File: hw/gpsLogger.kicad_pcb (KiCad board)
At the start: 2 copper layers, 41 x 72.8 mm, 163 parts, among them IC1 MSP430F55xx, P1 USB_OTG, P2 CONN_01X03, P3 CONN_01X03, Q1 Q_NMOS_AO8810, Q2 FG6943010R, SW1 SW_PUSH, SW2 SW_PUSH, U1 TPS27081A, U2 MCP73812, U3 uSD, U4 TPS27081A, U5 S8261, U6 TPS78230, X1 CRYSTAL_SMD

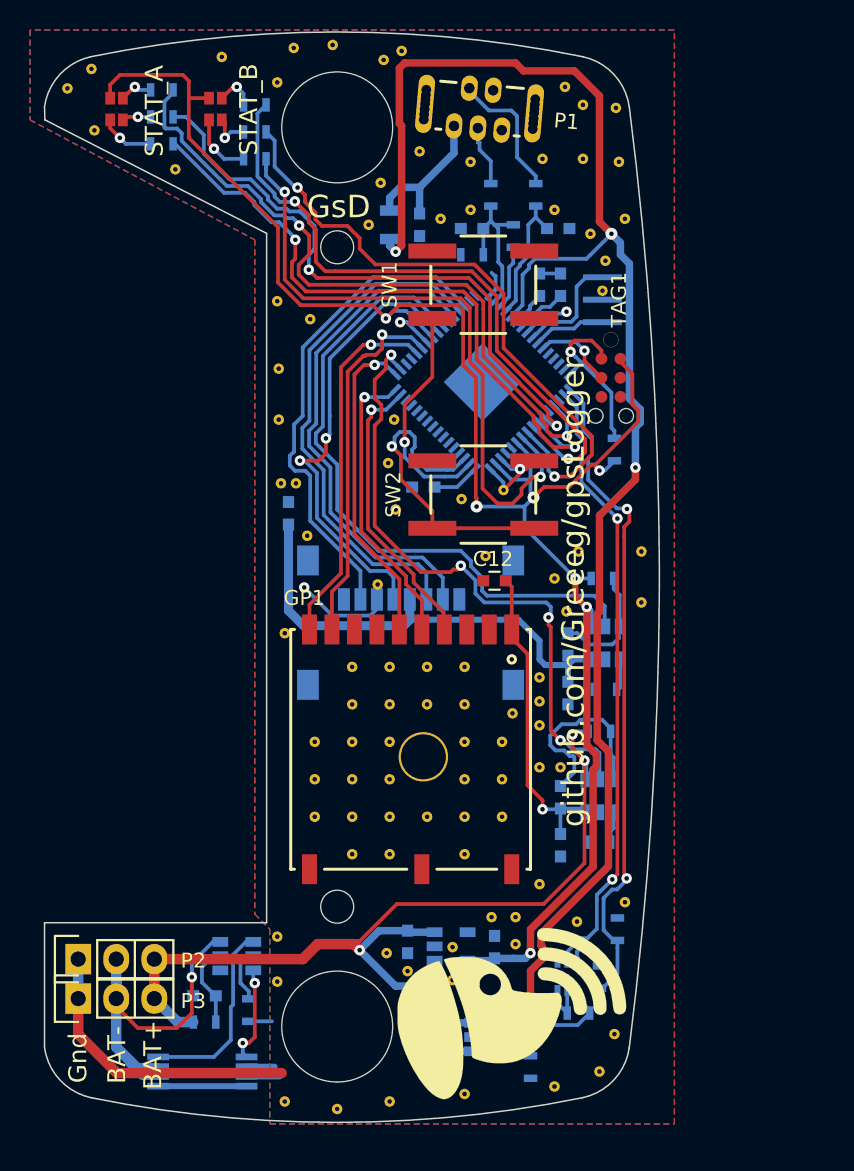
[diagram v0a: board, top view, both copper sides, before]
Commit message: 'Merge' Hardware changes mistakely made on Mark3 branch
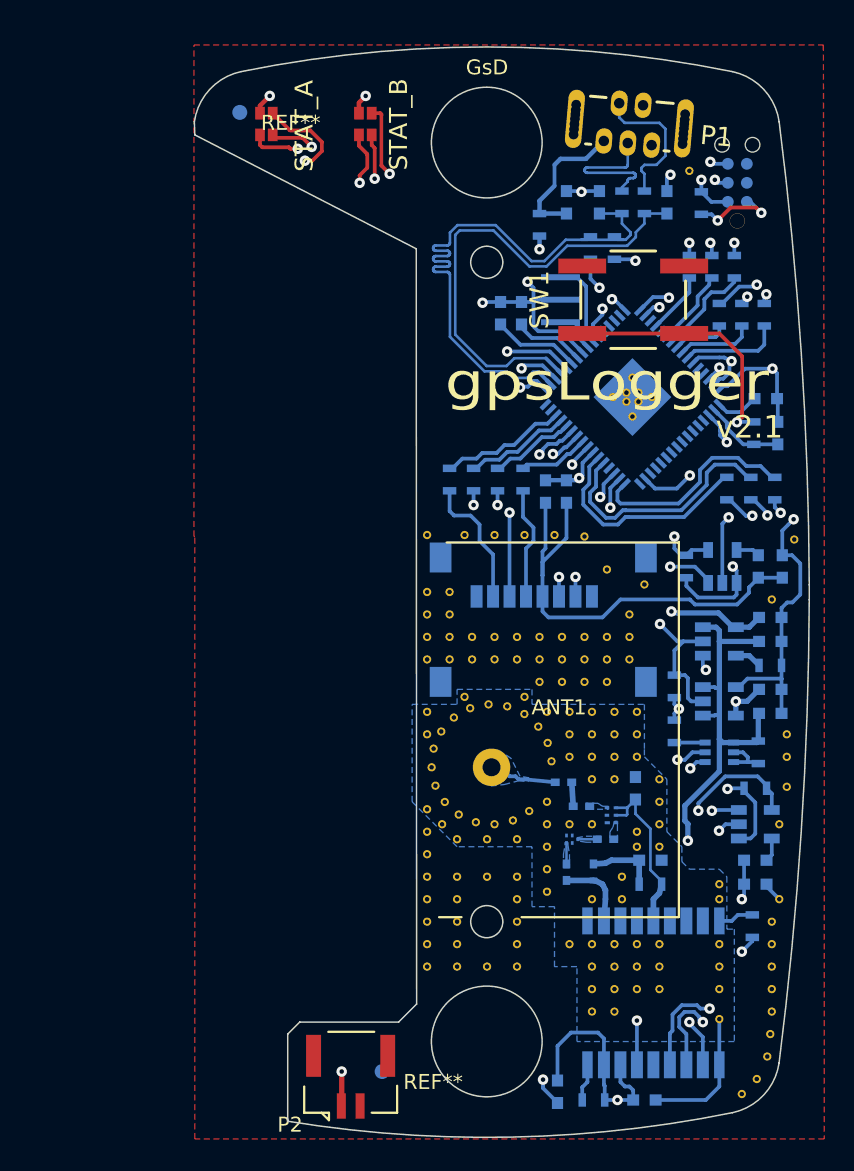
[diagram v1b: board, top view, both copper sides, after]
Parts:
- removed G*** (x2): LOGO, LOGO
- removed GP1: GPS, footprints:PA6C
- removed P3: CONN_01X03, Socket_Strips:Socket_Strip_Straight_1x03
- removed Q1: Q_NMOS_AO8810, Housings_SSOP:TSSOP-8_4.4x3mm_Pitch0.65mm
- removed the REF** at (160.7, 123.2)
- removed the REF** at (160.7, 77.6)
- removed the REF** at (141.5, 123.5)
- removed the REF** at (141.5, 79.5)
- removed the REF** at (141.5, 131.5)
- removed the REF** at (141.5, 71.5)
- removed the REF** at (160.1, 70.2)
- removed the REF** at (160.3, 73.8)
- removed the REF** at (157.9, 73.6)
- removed the REF** at (157.9, 70.0)
- removed the REF** at (156.7, 68.8)
- removed the REF** at (137.6, 87.6)
- removed the REF** at (137.6, 91.0)
- removed the REF** at (137.5, 83.1)
- removed the REF** at (139.7, 84.3)
- removed the REF** at (137.5, 68.5)
- removed the REF** at (145.3, 91.0)
- removed the REF** at (144.9, 93.9)
- removed the REF** at (145.4, 97.0)
- removed the REF** at (149.8, 96.3)
- removed the REF** at (152.6, 95.7)
- removed the REF** at (157.5, 124.5)
- removed the REF** at (155.0, 122.0)
- removed the REF** at (137.5, 125.5)
- removed the REF** at (137.5, 128.5)
- removed the REF** at (160.0, 132.0)
- removed the REF** at (130.7, 74.3)
- removed the REF** at (159.0, 134.5)
- removed the REF** at (156.0, 135.5)
- removed the REF** at (150.0, 136.0)
- removed the REF** at (145.0, 136.5)
- removed the REF** at (141.5, 137.0)
- removed the REF** at (138.0, 136.5)
- removed the REF** at (150.0, 107.5)
- removed the REF** at (152.5, 115.0)
- removed the REF** at (152.5, 112.5)
- removed the REF** at (145.0, 112.5)
- removed the REF** at (125.3, 71.7)
- removed the REF** at (142.5, 112.5)
- removed the REF** at (140.0, 112.5)
- removed the REF** at (142.5, 110.0)
- removed the REF** at (145.0, 110.0)
- removed the REF** at (147.5, 110.0)
- removed the REF** at (150.0, 110.0)
- removed the REF** at (150.0, 112.5)
- removed the REF** at (150.0, 115.0)
- removed the REF** at (145.0, 115.0)
- removed the REF** at (142.5, 115.0)
- removed the REF** at (123.5, 68.9)
- removed the REF** at (152.5, 117.5)
- removed the REF** at (150.0, 117.5)
- removed the REF** at (147.5, 117.5)
- removed the REF** at (145.0, 117.5)
- removed the REF** at (142.5, 117.5)
- removed the REF** at (145.0, 120.0)
- removed the REF** at (142.5, 120.0)
- removed the REF** at (138.6, 66.2)
- removed the REF** at (141.2, 66.0)
- removed the REF** at (145.8, 66.4)
- removed the REF** at (125.1, 67.6)
- removed the REF** at (144.6, 67.0)
- removed the REF** at (144.4, 75.2)
- removed the REF** at (143.6, 78.0)
- removed the REF** at (155.2, 73.6)
- removed the REF** at (150.4, 73.8)
- removed the REF** at (150.4, 77.0)
- removed the REF** at (156.0, 77.0)
- removed the REF** at (158.4, 78.6)
- removed the REF** at (159.2, 82.4)
- removed the REF** at (159.4, 80.4)
- removed the REF** at (133.8, 66.8)
- removed the REF** at (156.0, 101.6)
- removed the REF** at (157.6, 99.8)
- removed the REF** at (161.8, 103.2)
- removed the REF** at (161.8, 99.8)
- removed the REF** at (156.8, 103.8)
- removed the REF** at (150.0, 120.0)
- removed the REF** at (153.2, 110.6)
- removed the REF** at (155.0, 114.2)
- removed the REF** at (156.4, 114.2)
- removed the REF** at (155.0, 111.4)
- removed the REF** at (148.4, 77.6)
- removed the REF** at (155.0, 109.8)
- removed the REF** at (155.0, 108.2)
- removed the REF** at (153.4, 124.2)
- removed the REF** at (153.4, 126.0)
- removed the REF** at (151.8, 124.2)
- removed the REF** at (149.2, 128.4)
- removed the REF** at (149.2, 126.2)
- removed the REF** at (146.2, 127.8)
- removed the REF** at (144.8, 126.6)
- removed the REF** at (147.5, 107.5)
- removed the REF** at (147.0, 73.1)
- removed the REF** at (142.5, 107.5)
- removed the REF** at (145.0, 107.5)
- removed the REF** at (138.0, 105.2)
- removed the REF** at (137.8, 95.2)
- removed the REF** at (138.8, 95.2)
- removed the REF** at (139.5, 98.8)
- removed the REF** at (151.4, 100.1)
- removed the REF** at (144.2, 102.0)
- removed the REF** at (140.0, 115.0)
- removed the REF** at (140.0, 117.5)
- removed SW2: SW_PUSH, cameraTrigger_rev1_0:EVQ_switch
- added ANT1: ANT, footprints:GPS_ANT, F.Cu at (151.8, 114.2)
- added C18: 100n, Capacitors_SMD:C_0603, B.Cu at (155.4, 95.8)
- added C19: 47pF, Capacitors_SMD:C_0402, B.Cu at (156.6, 115.2)
- added C20: 1nF, Capacitors_SMD:C_0603, B.Cu at (161.4, 115.6)
- added C21: 47pF, Capacitors_SMD:C_0402, B.Cu at (159.4, 119.0)
- added C22: 47pF, Capacitors_SMD:C_0402, B.Cu at (156.8, 121.2)
- added FLT1: B8813, footprints:SAW-5, B.Cu at (157.2, 119.0)
- added L1: 27nH, Capacitors_SMD:C_0402, B.Cu at (158.6, 121.2)
- added L2: 100nH, Capacitors_SMD:C_0603, B.Cu at (169.4, 120.4)
- added L3: 100nH, Capacitors_SMD:C_0603, B.Cu at (169.6, 100.8)
- added L4: 5.6nH, Capacitors_SMD:C_0402, B.Cu at (157.8, 116.8)
- added R22: 2k2, Resistors_SMD:R_0603, B.Cu at (149.0, 95.0)
- added R23: 2k2, Resistors_SMD:R_0603, B.Cu at (150.6, 95.0)
- added R24: 2k2, Resistors_SMD:R_0603, B.Cu at (152.2, 95.0)
- added R25: 2k2, Resistors_SMD:R_0603, B.Cu at (153.9, 95.0)
- added R26: 2k2, Resistors_SMD:R_0603, B.Cu at (167.5, 95.6)
- added R27: 2k2, Resistors_SMD:R_0603, B.Cu at (169.1, 95.6)
- added R28: 2k2, Resistors_SMD:R_0603, B.Cu at (170.7, 95.6)
- added REF**: Fiducial_1mm_Dia_2.54mm_Outer_CopperBottom, Fiducials:Fiducial_1mm_Dia_2.54mm_Outer_CopperBottom, F.Cu at (144.5, 134.5)
- added REF**: SolderWirePad_single_0-8mmDrill, Wire_Pads:SolderWirePad_single_0-8mmDrill, F.Cu at (165.0, 74.4)
- added REF**: Fiducial_1mm_Dia_2.54mm_Outer_CopperBottom, Fiducials:Fiducial_1mm_Dia_2.54mm_Outer_CopperBottom, F.Cu at (135.0, 70.5)
- added REF**1: SolderWirePad_single_0-8mmDrill, Wire_Pads:SolderWirePad_single_0-8mmDrill, F.Cu at (160.8, 89.8)
- added REF**1: SolderWirePad_single_0-8mmDrill, Wire_Pads:SolderWirePad_single_0-8mmDrill, F.Cu at (155.0, 108.5)
- added REF**1: SolderWirePad_single_0-8mmDrill, Wire_Pads:SolderWirePad_single_0-8mmDrill, F.Cu at (147.5, 117.0)
- added REF**1: SolderWirePad_single_0-8mmDrill, Wire_Pads:SolderWirePad_single_0-8mmDrill, F.Cu at (148.5, 118.0)
- added REF**1: SolderWirePad_single_0-8mmDrill, Wire_Pads:SolderWirePad_single_0-8mmDrill, F.Cu at (149.5, 119.0)
- added REF**1: SolderWirePad_single_0-8mmDrill, Wire_Pads:SolderWirePad_single_0-8mmDrill, F.Cu at (151.5, 119.0)
- added REF**1: SolderWirePad_single_0-8mmDrill, Wire_Pads:SolderWirePad_single_0-8mmDrill, F.Cu at (153.5, 119.0)
- added REF**1: SolderWirePad_single_0-8mmDrill, Wire_Pads:SolderWirePad_single_0-8mmDrill, F.Cu at (155.5, 122.5)
- added REF**1: SolderWirePad_single_0-8mmDrill, Wire_Pads:SolderWirePad_single_0-8mmDrill, F.Cu at (155.5, 121.0)
- added REF**1: SolderWirePad_single_0-8mmDrill, Wire_Pads:SolderWirePad_single_0-8mmDrill, F.Cu at (155.5, 119.5)
- added REF**1: SolderWirePad_single_0-8mmDrill, Wire_Pads:SolderWirePad_single_0-8mmDrill, F.Cu at (158.5, 123.0)
- added REF**1: SolderWirePad_single_0-8mmDrill, Wire_Pads:SolderWirePad_single_0-8mmDrill, F.Cu at (160.5, 121.5)
- added REF**1: SolderWirePad_single_0-8mmDrill, Wire_Pads:SolderWirePad_single_0-8mmDrill, F.Cu at (159.5, 108.5)
- added REF**1: SolderWirePad_single_0-8mmDrill, Wire_Pads:SolderWirePad_single_0-8mmDrill, F.Cu at (160.5, 123.0)
- added REF**1: SolderWirePad_single_0-8mmDrill, Wire_Pads:SolderWirePad_single_0-8mmDrill, F.Cu at (155.5, 116.5)
- added REF**1: SolderWirePad_single_0-8mmDrill, Wire_Pads:SolderWirePad_single_0-8mmDrill, F.Cu at (155.5, 118.0)
- added REF**1: SolderWirePad_single_0-8mmDrill, Wire_Pads:SolderWirePad_single_0-8mmDrill, F.Cu at (157.0, 118.0)
- added REF**1: SolderWirePad_single_0-8mmDrill, Wire_Pads:SolderWirePad_single_0-8mmDrill, F.Cu at (158.5, 118.0)
- added REF**1: SolderWirePad_single_0-8mmDrill, Wire_Pads:SolderWirePad_single_0-8mmDrill, F.Cu at (161.5, 118.5)
- added REF**1: SolderWirePad_single_0-8mmDrill, Wire_Pads:SolderWirePad_single_0-8mmDrill, F.Cu at (161.5, 119.5)
- added REF**1: SolderWirePad_single_0-8mmDrill, Wire_Pads:SolderWirePad_single_0-8mmDrill, F.Cu at (163.0, 119.5)
- added REF**1: SolderWirePad_single_0-8mmDrill, Wire_Pads:SolderWirePad_single_0-8mmDrill, F.Cu at (163.0, 118.0)
- added REF**1: SolderWirePad_single_0-8mmDrill, Wire_Pads:SolderWirePad_single_0-8mmDrill, F.Cu at (163.0, 116.5)
- added REF**1: SolderWirePad_single_0-8mmDrill, Wire_Pads:SolderWirePad_single_0-8mmDrill, F.Cu at (158.0, 108.5)
- added REF**1: SolderWirePad_single_0-8mmDrill, Wire_Pads:SolderWirePad_single_0-8mmDrill, F.Cu at (163.0, 115.0)
- added REF**1: SolderWirePad_single_0-8mmDrill, Wire_Pads:SolderWirePad_single_0-8mmDrill, F.Cu at (160.0, 115.0)
- added REF**1: SolderWirePad_single_0-8mmDrill, Wire_Pads:SolderWirePad_single_0-8mmDrill, F.Cu at (158.5, 115.0)
- added REF**1: SolderWirePad_single_0-8mmDrill, Wire_Pads:SolderWirePad_single_0-8mmDrill, F.Cu at (157.0, 113.5)
- added REF**1: SolderWirePad_single_0-8mmDrill, Wire_Pads:SolderWirePad_single_0-8mmDrill, F.Cu at (158.5, 113.5)
- added REF**1: SolderWirePad_single_0-8mmDrill, Wire_Pads:SolderWirePad_single_0-8mmDrill, F.Cu at (160.0, 113.5)
- added REF**1: SolderWirePad_single_0-8mmDrill, Wire_Pads:SolderWirePad_single_0-8mmDrill, F.Cu at (161.5, 113.5)
- added REF**1: SolderWirePad_single_0-8mmDrill, Wire_Pads:SolderWirePad_single_0-8mmDrill, F.Cu at (161.5, 112.0)
- added REF**1: SolderWirePad_single_0-8mmDrill, Wire_Pads:SolderWirePad_single_0-8mmDrill, F.Cu at (160.0, 112.0)
- added REF**1: SolderWirePad_single_0-8mmDrill, Wire_Pads:SolderWirePad_single_0-8mmDrill, F.Cu at (158.5, 112.0)
- added REF**1: SolderWirePad_single_0-8mmDrill, Wire_Pads:SolderWirePad_single_0-8mmDrill, F.Cu at (149.0, 102.5)
- added REF**1: SolderWirePad_single_0-8mmDrill, Wire_Pads:SolderWirePad_single_0-8mmDrill, F.Cu at (157.0, 112.0)
- added REF**1: SolderWirePad_single_0-8mmDrill, Wire_Pads:SolderWirePad_single_0-8mmDrill, F.Cu at (155.5, 110.5)
- added REF**1: SolderWirePad_single_0-8mmDrill, Wire_Pads:SolderWirePad_single_0-8mmDrill, F.Cu at (157.0, 110.5)
- added REF**1: SolderWirePad_single_0-8mmDrill, Wire_Pads:SolderWirePad_single_0-8mmDrill, F.Cu at (158.5, 110.5)
- added REF**1: SolderWirePad_single_0-8mmDrill, Wire_Pads:SolderWirePad_single_0-8mmDrill, F.Cu at (160.0, 110.5)
- added REF**1: SolderWirePad_single_0-8mmDrill, Wire_Pads:SolderWirePad_single_0-8mmDrill, F.Cu at (161.5, 110.5)
- added REF**1: SolderWirePad_single_0-8mmDrill, Wire_Pads:SolderWirePad_single_0-8mmDrill, F.Cu at (158.0, 98.8)
- added REF**1: SolderWirePad_single_0-8mmDrill, Wire_Pads:SolderWirePad_single_0-8mmDrill, F.Cu at (156.0, 98.7)
- added REF**1: SolderWirePad_single_0-8mmDrill, Wire_Pads:SolderWirePad_single_0-8mmDrill, F.Cu at (154.0, 98.7)
- added REF**1: SolderWirePad_single_0-8mmDrill, Wire_Pads:SolderWirePad_single_0-8mmDrill, F.Cu at (152.0, 98.7)
- added REF**1: SolderWirePad_single_0-8mmDrill, Wire_Pads:SolderWirePad_single_0-8mmDrill, F.Cu at (147.5, 102.5)
- added REF**1: SolderWirePad_single_0-8mmDrill, Wire_Pads:SolderWirePad_single_0-8mmDrill, F.Cu at (150.0, 98.7)
- added REF**1: SolderWirePad_single_0-8mmDrill, Wire_Pads:SolderWirePad_single_0-8mmDrill, F.Cu at (147.5, 98.7)
- added REF**1: SolderWirePad_single_0-8mmDrill, Wire_Pads:SolderWirePad_single_0-8mmDrill, F.Cu at (147.8, 114.2)
- added REF**1: SolderWirePad_single_0-8mmDrill, Wire_Pads:SolderWirePad_single_0-8mmDrill, F.Cu at (147.5, 104.0)
- added REF**1: SolderWirePad_single_0-8mmDrill, Wire_Pads:SolderWirePad_single_0-8mmDrill, F.Cu at (149.0, 104.0)
- added REF**1: SolderWirePad_single_0-8mmDrill, Wire_Pads:SolderWirePad_single_0-8mmDrill, F.Cu at (161.0, 104.0)
- added REF**1: SolderWirePad_single_0-8mmDrill, Wire_Pads:SolderWirePad_single_0-8mmDrill, F.Cu at (147.5, 107.0)
- added REF**1: SolderWirePad_single_0-8mmDrill, Wire_Pads:SolderWirePad_single_0-8mmDrill, F.Cu at (159.5, 107.0)
- added REF**1: SolderWirePad_single_0-8mmDrill, Wire_Pads:SolderWirePad_single_0-8mmDrill, F.Cu at (161.6, 89.8)
- added REF**1: SolderWirePad_single_0-8mmDrill, Wire_Pads:SolderWirePad_single_0-8mmDrill, F.Cu at (158.0, 107.0)
- added REF**1: SolderWirePad_single_0-8mmDrill, Wire_Pads:SolderWirePad_single_0-8mmDrill, F.Cu at (156.5, 107.0)
- added REF**1: SolderWirePad_single_0-8mmDrill, Wire_Pads:SolderWirePad_single_0-8mmDrill, F.Cu at (155.0, 107.0)
- added REF**1: SolderWirePad_single_0-8mmDrill, Wire_Pads:SolderWirePad_single_0-8mmDrill, F.Cu at (153.5, 107.0)
- added REF**1: SolderWirePad_single_0-8mmDrill, Wire_Pads:SolderWirePad_single_0-8mmDrill, F.Cu at (152.0, 107.0)
- added REF**1: SolderWirePad_single_0-8mmDrill, Wire_Pads:SolderWirePad_single_0-8mmDrill, F.Cu at (150.5, 107.0)
- added REF**1: SolderWirePad_single_0-8mmDrill, Wire_Pads:SolderWirePad_single_0-8mmDrill, F.Cu at (149.0, 107.0)
- added REF**1: SolderWirePad_single_0-8mmDrill, Wire_Pads:SolderWirePad_single_0-8mmDrill, F.Cu at (161.0, 107.0)
- added REF**1: SolderWirePad_single_0-8mmDrill, Wire_Pads:SolderWirePad_single_0-8mmDrill, F.Cu at (161.0, 105.5)
- added REF**1: SolderWirePad_single_0-8mmDrill, Wire_Pads:SolderWirePad_single_0-8mmDrill, F.Cu at (159.5, 105.5)
- added REF**1: SolderWirePad_single_0-8mmDrill, Wire_Pads:SolderWirePad_single_0-8mmDrill, F.Cu at (161.6, 89.2)
- added REF**1: SolderWirePad_single_0-8mmDrill, Wire_Pads:SolderWirePad_single_0-8mmDrill, F.Cu at (158.0, 105.5)
- added REF**1: SolderWirePad_single_0-8mmDrill, Wire_Pads:SolderWirePad_single_0-8mmDrill, F.Cu at (156.5, 105.5)
- added REF**1: SolderWirePad_single_0-8mmDrill, Wire_Pads:SolderWirePad_single_0-8mmDrill, F.Cu at (155.0, 105.5)
- added REF**1: SolderWirePad_single_0-8mmDrill, Wire_Pads:SolderWirePad_single_0-8mmDrill, F.Cu at (153.5, 105.5)
- added REF**1: SolderWirePad_single_0-8mmDrill, Wire_Pads:SolderWirePad_single_0-8mmDrill, F.Cu at (152.0, 105.5)
- added REF**1: SolderWirePad_single_0-8mmDrill, Wire_Pads:SolderWirePad_single_0-8mmDrill, F.Cu at (150.5, 105.5)
- added REF**1: SolderWirePad_single_0-8mmDrill, Wire_Pads:SolderWirePad_single_0-8mmDrill, F.Cu at (149.0, 105.5)
- added REF**1: SolderWirePad_single_0-8mmDrill, Wire_Pads:SolderWirePad_single_0-8mmDrill, F.Cu at (147.5, 105.5)
- added REF**1: SolderWirePad_single_0-8mmDrill, Wire_Pads:SolderWirePad_single_0-8mmDrill, F.Cu at (149.5, 124.5)
- added REF**1: SolderWirePad_single_0-8mmDrill, Wire_Pads:SolderWirePad_single_0-8mmDrill, F.Cu at (149.5, 123.0)
- added REF**1: SolderWirePad_single_0-8mmDrill, Wire_Pads:SolderWirePad_single_0-8mmDrill, F.Cu at (160.8, 89.2)
- added REF**1: SolderWirePad_single_0-8mmDrill, Wire_Pads:SolderWirePad_single_0-8mmDrill, F.Cu at (149.5, 121.5)
- added REF**1: SolderWirePad_single_0-8mmDrill, Wire_Pads:SolderWirePad_single_0-8mmDrill, F.Cu at (151.5, 121.5)
- added REF**1: SolderWirePad_single_0-8mmDrill, Wire_Pads:SolderWirePad_single_0-8mmDrill, F.Cu at (153.5, 121.5)
- added REF**1: SolderWirePad_single_0-8mmDrill, Wire_Pads:SolderWirePad_single_0-8mmDrill, F.Cu at (153.5, 123.0)
- added REF**1: SolderWirePad_single_0-8mmDrill, Wire_Pads:SolderWirePad_single_0-8mmDrill, F.Cu at (153.5, 124.5)
- added REF**1: SolderWirePad_single_0-8mmDrill, Wire_Pads:SolderWirePad_single_0-8mmDrill, F.Cu at (153.5, 126.0)
- added REF**1: SolderWirePad_single_0-8mmDrill, Wire_Pads:SolderWirePad_single_0-8mmDrill, F.Cu at (149.5, 126.0)
- added REF**1: SolderWirePad_single_0-8mmDrill, Wire_Pads:SolderWirePad_single_0-8mmDrill, F.Cu at (147.5, 118.5)
- added REF**1: SolderWirePad_single_0-8mmDrill, Wire_Pads:SolderWirePad_single_0-8mmDrill, F.Cu at (147.5, 120.0)
- added REF**1: SolderWirePad_single_0-8mmDrill, Wire_Pads:SolderWirePad_single_0-8mmDrill, F.Cu at (147.5, 121.5)
- added REF**1: SolderWirePad_single_0-8mmDrill, Wire_Pads:SolderWirePad_single_0-8mmDrill, F.Cu at (161.2, 90.8)
- added REF**1: SolderWirePad_single_0-8mmDrill, Wire_Pads:SolderWirePad_single_0-8mmDrill, F.Cu at (147.5, 123.0)
- added REF**1: SolderWirePad_single_0-8mmDrill, Wire_Pads:SolderWirePad_single_0-8mmDrill, F.Cu at (147.5, 124.5)
- added REF**1: SolderWirePad_single_0-8mmDrill, Wire_Pads:SolderWirePad_single_0-8mmDrill, F.Cu at (147.5, 126.0)
- added REF**1: SolderWirePad_single_0-8mmDrill, Wire_Pads:SolderWirePad_single_0-8mmDrill, F.Cu at (147.5, 127.5)
- added REF**1: SolderWirePad_single_0-8mmDrill, Wire_Pads:SolderWirePad_single_0-8mmDrill, F.Cu at (149.5, 127.5)
- added REF**1: SolderWirePad_single_0-8mmDrill, Wire_Pads:SolderWirePad_single_0-8mmDrill, F.Cu at (151.5, 127.5)
- added REF**1: SolderWirePad_single_0-8mmDrill, Wire_Pads:SolderWirePad_single_0-8mmDrill, F.Cu at (153.5, 127.5)
- added REF**1: SolderWirePad_single_0-8mmDrill, Wire_Pads:SolderWirePad_single_0-8mmDrill, F.Cu at (168.5, 136.0)
- added REF**1: SolderWirePad_single_0-8mmDrill, Wire_Pads:SolderWirePad_single_0-8mmDrill, F.Cu at (169.5, 135.0)
- added REF**1: SolderWirePad_single_0-8mmDrill, Wire_Pads:SolderWirePad_single_0-8mmDrill, F.Cu at (170.2, 133.5)
- added REF**1: SolderWirePad_single_0-8mmDrill, Wire_Pads:SolderWirePad_single_0-8mmDrill, F.Cu at (161.2, 88.2)
- added REF**1: SolderWirePad_single_0-8mmDrill, Wire_Pads:SolderWirePad_single_0-8mmDrill, F.Cu at (170.4, 132.0)
- added REF**1: SolderWirePad_single_0-8mmDrill, Wire_Pads:SolderWirePad_single_0-8mmDrill, F.Cu at (170.5, 130.5)
- added REF**1: SolderWirePad_single_0-8mmDrill, Wire_Pads:SolderWirePad_single_0-8mmDrill, F.Cu at (170.5, 129.0)
- added REF**1: SolderWirePad_single_0-8mmDrill, Wire_Pads:SolderWirePad_single_0-8mmDrill, F.Cu at (170.5, 127.5)
- added REF**1: SolderWirePad_single_0-8mmDrill, Wire_Pads:SolderWirePad_single_0-8mmDrill, F.Cu at (170.5, 126.0)
- added REF**1: SolderWirePad_single_0-8mmDrill, Wire_Pads:SolderWirePad_single_0-8mmDrill, F.Cu at (170.5, 124.5)
- added REF**1: SolderWirePad_single_0-8mmDrill, Wire_Pads:SolderWirePad_single_0-8mmDrill, F.Cu at (171.0, 123.0)
- added REF**1: SolderWirePad_single_0-8mmDrill, Wire_Pads:SolderWirePad_single_0-8mmDrill, F.Cu at (171.0, 118.0)
- added REF**1: SolderWirePad_single_0-8mmDrill, Wire_Pads:SolderWirePad_single_0-8mmDrill, F.Cu at (171.5, 115.5)
- added REF**1: SolderWirePad_single_0-8mmDrill, Wire_Pads:SolderWirePad_single_0-8mmDrill, F.Cu at (171.5, 113.5)
- added REF**1: SolderWirePad_single_0-8mmDrill, Wire_Pads:SolderWirePad_single_0-8mmDrill, F.Cu at (162.5, 89.5)
- added REF**1: SolderWirePad_single_0-8mmDrill, Wire_Pads:SolderWirePad_single_0-8mmDrill, F.Cu at (171.5, 112.0)
- added REF**1: SolderWirePad_single_0-8mmDrill, Wire_Pads:SolderWirePad_single_0-8mmDrill, F.Cu at (172.0, 99.0)
- added REF**1: SolderWirePad_single_0-8mmDrill, Wire_Pads:SolderWirePad_single_0-8mmDrill, F.Cu at (170.5, 103.0)
- added REF**1: SolderWirePad_single_0-8mmDrill, Wire_Pads:SolderWirePad_single_0-8mmDrill, F.Cu at (159.5, 101.0)
- added REF**1: SolderWirePad_single_0-8mmDrill, Wire_Pads:SolderWirePad_single_0-8mmDrill, F.Cu at (162.0, 102.0)
- added REF**1: SolderWirePad_single_0-8mmDrill, Wire_Pads:SolderWirePad_single_0-8mmDrill, F.Cu at (158.5, 130.5)
- added REF**1: SolderWirePad_single_0-8mmDrill, Wire_Pads:SolderWirePad_single_0-8mmDrill, F.Cu at (160.0, 130.5)
- added REF**1: SolderWirePad_single_0-8mmDrill, Wire_Pads:SolderWirePad_single_0-8mmDrill, F.Cu at (158.5, 129.0)
- added REF**1: SolderWirePad_single_0-8mmDrill, Wire_Pads:SolderWirePad_single_0-8mmDrill, F.Cu at (167.0, 129.0)
- added REF**1: SolderWirePad_single_0-8mmDrill, Wire_Pads:SolderWirePad_single_0-8mmDrill, F.Cu at (160.0, 129.0)
- added REF**1: SolderWirePad_single_0-8mmDrill, Wire_Pads:SolderWirePad_single_0-8mmDrill, F.Cu at (159.9, 89.5)
- added REF**1: SolderWirePad_single_0-8mmDrill, Wire_Pads:SolderWirePad_single_0-8mmDrill, F.Cu at (163.0, 129.0)
- added REF**1: SolderWirePad_single_0-8mmDrill, Wire_Pads:SolderWirePad_single_0-8mmDrill, F.Cu at (161.5, 129.0)
- added REF**1: SolderWirePad_single_0-8mmDrill, Wire_Pads:SolderWirePad_single_0-8mmDrill, F.Cu at (157.0, 126.0)
- added REF**1: SolderWirePad_single_0-8mmDrill, Wire_Pads:SolderWirePad_single_0-8mmDrill, F.Cu at (158.5, 127.5)
- added REF**1: SolderWirePad_single_0-8mmDrill, Wire_Pads:SolderWirePad_single_0-8mmDrill, F.Cu at (158.5, 126.0)
- added REF**1: SolderWirePad_single_0-8mmDrill, Wire_Pads:SolderWirePad_single_0-8mmDrill, F.Cu at (160.0, 127.5)
- added REF**1: SolderWirePad_single_0-8mmDrill, Wire_Pads:SolderWirePad_single_0-8mmDrill, F.Cu at (160.0, 126.0)
- added REF**1: SolderWirePad_single_0-8mmDrill, Wire_Pads:SolderWirePad_single_0-8mmDrill, F.Cu at (161.5, 127.5)
- added REF**1: SolderWirePad_single_0-8mmDrill, Wire_Pads:SolderWirePad_single_0-8mmDrill, F.Cu at (161.5, 126.0)
- added REF**1: SolderWirePad_single_0-8mmDrill, Wire_Pads:SolderWirePad_single_0-8mmDrill, F.Cu at (163.0, 127.5)
- added REF**1: SolderWirePad_single_0-8mmDrill, Wire_Pads:SolderWirePad_single_0-8mmDrill, F.Cu at (156.5, 108.5)
- added REF**1: SolderWirePad_single_0-8mmDrill, Wire_Pads:SolderWirePad_single_0-8mmDrill, F.Cu at (163.0, 126.0)
- added REF**1: SolderWirePad_single_0-8mmDrill, Wire_Pads:SolderWirePad_single_0-8mmDrill, F.Cu at (167.0, 131.0)
- added REF**1: SolderWirePad_single_0-8mmDrill, Wire_Pads:SolderWirePad_single_0-8mmDrill, F.Cu at (167.0, 127.5)
- added REF**1: SolderWirePad_single_0-8mmDrill, Wire_Pads:SolderWirePad_single_0-8mmDrill, F.Cu at (167.0, 126.0)
- added REF**1: SolderWirePad_single_0-8mmDrill, Wire_Pads:SolderWirePad_single_0-8mmDrill, F.Cu at (167.0, 123.0)
- added REF**1: SolderWirePad_single_0-8mmDrill, Wire_Pads:SolderWirePad_single_0-8mmDrill, F.Cu at (167.0, 122.0)
- added REF**1: SolderWirePad_single_0-8mmDrill, Wire_Pads:SolderWirePad_single_0-8mmDrill, F.Cu at (154.0, 109.5)
- added REF**1: SolderWirePad_single_0-8mmDrill, Wire_Pads:SolderWirePad_single_0-8mmDrill, F.Cu at (150.0, 109.5)
- added REF**1: SolderWirePad_single_0-8mmDrill, Wire_Pads:SolderWirePad_single_0-8mmDrill, F.Cu at (147.5, 112.0)
- added REF**1: SolderWirePad_single_0-8mmDrill, Wire_Pads:SolderWirePad_single_0-8mmDrill, F.Cu at (147.5, 110.5)
- added REF**11: SolderWirePad_single_0-8mmDrill, Wire_Pads:SolderWirePad_single_0-8mmDrill, F.Cu at (155.8, 113.8)
- added REF**12: SolderWirePad_single_0-8mmDrill, Wire_Pads:SolderWirePad_single_0-8mmDrill, F.Cu at (155.5, 112.6)
- added REF**13: SolderWirePad_single_0-8mmDrill, Wire_Pads:SolderWirePad_single_0-8mmDrill, F.Cu at (154.9, 111.5)
- added REF**14: SolderWirePad_single_0-8mmDrill, Wire_Pads:SolderWirePad_single_0-8mmDrill, F.Cu at (154.0, 110.6)
- added REF**15: SolderWirePad_single_0-8mmDrill, Wire_Pads:SolderWirePad_single_0-8mmDrill, F.Cu at (152.8, 110.1)
- added REF**16: SolderWirePad_single_0-8mmDrill, Wire_Pads:SolderWirePad_single_0-8mmDrill, F.Cu at (151.6, 110.0)
- added REF**17: SolderWirePad_single_0-8mmDrill, Wire_Pads:SolderWirePad_single_0-8mmDrill, F.Cu at (150.4, 110.3)
- added REF**18: SolderWirePad_single_0-8mmDrill, Wire_Pads:SolderWirePad_single_0-8mmDrill, F.Cu at (149.3, 110.9)
- added REF**19: SolderWirePad_single_0-8mmDrill, Wire_Pads:SolderWirePad_single_0-8mmDrill, F.Cu at (148.4, 111.8)
- added REF**2: SolderWirePad_single_0-8mmDrill, Wire_Pads:SolderWirePad_single_0-8mmDrill, F.Cu at (148.1, 115.4)
- added REF**20: SolderWirePad_single_0-8mmDrill, Wire_Pads:SolderWirePad_single_0-8mmDrill, F.Cu at (147.9, 113.0)
- added REF**3: SolderWirePad_single_0-8mmDrill, Wire_Pads:SolderWirePad_single_0-8mmDrill, F.Cu at (148.7, 116.5)
- added REF**4: SolderWirePad_single_0-8mmDrill, Wire_Pads:SolderWirePad_single_0-8mmDrill, F.Cu at (149.6, 117.4)
- added REF**5: SolderWirePad_single_0-8mmDrill, Wire_Pads:SolderWirePad_single_0-8mmDrill, F.Cu at (150.8, 117.9)
- added REF**6: SolderWirePad_single_0-8mmDrill, Wire_Pads:SolderWirePad_single_0-8mmDrill, F.Cu at (152.0, 118.0)
- added REF**7: SolderWirePad_single_0-8mmDrill, Wire_Pads:SolderWirePad_single_0-8mmDrill, F.Cu at (153.2, 117.7)
- added REF**8: SolderWirePad_single_0-8mmDrill, Wire_Pads:SolderWirePad_single_0-8mmDrill, F.Cu at (154.3, 117.1)
- added U7: BGU7007, footprints:XSON6, B.Cu at (159.8, 117.4)
- C1, C5, C7: value C -> 10n
- C10, C11: value C -> 100n
- C12: value C -> 10n; moved to B.Cu
- C13, C16, C17, C4, C8: value C -> 1uF
- C2, C3: value C -> 22p
- FB1: value FILTER -> 1k FB; footprint Resistors_SMD:R_0805 -> Resistors_SMD:R_0603
- P2: value CONN_01X03 -> CONN_01X02; footprint Socket_Strips:Socket_Strip_Straight_1x03 -> footprints:BM02B-GHS-TBT
- R1, R2: value R -> 27R
- R10: value R -> 1k
- R11: value 1K -> 10k
- R3: value R -> 470k
- R4: value R -> 1k4
- R5, R8: value R -> 10k
- R6: value R -> 10R
- R9: value 330R -> 10k
- TAG1: moved to B.Cu
- U1: value TPS27081A -> MAX_M8Q; footprint TO_SOT_Packages_SMD:SOT-23-6 -> footprints:MAX_M8
- U4: value TPS27081A -> MIC2091; footprint TO_SOT_Packages_SMD:SOT-23-6 -> TO_SOT_Packages_SMD:SOT-23-5
- U5: value S8261 -> MIC2091; footprint TO_SOT_Packages_SMD:SOT-23-6 -> TO_SOT_Packages_SMD:SOT-23-5
- moved C11 53.6 mm to (170.9, 91.9), turned to 90 degrees
- moved R11 41.6 mm to (164.8, 100.8)
- moved U5 41.5 mm to (167.2, 100.8), turned to 90 degrees
- moved R9 39.9 mm to (169.4, 115.6)
- moved R18 39.1 mm to (168.0, 80.8), turned to 270 degrees
- moved R17 38.0 mm to (166.5, 80.8), turned to 270 degrees
- moved C6 37.1 mm to (170.4, 104.2), turned to 0 degrees
- moved R16 37.1 mm to (165.0, 80.8), turned to 270 degrees
- moved C12 36.1 mm to (162.0, 136.4), turned to 0 degrees
- moved R21 35.6 mm to (170.0, 84.0), turned to 270 degrees
- moved R20 34.7 mm to (168.5, 84.0), turned to 270 degrees
- moved R19 34.0 mm to (167.0, 84.0), turned to 270 degrees
- moved C9 33.8 mm to (170.4, 105.8), turned to 0 degrees
- moved R7 31.2 mm to (170.4, 107.4), turned to 180 degrees
- moved U2 30.6 mm to (167.0, 105.8)
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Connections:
- net /D+ renamed /USB_IN_P
- net /D- renamed /USB_IN_N
- net /DM renamed /USB_DATA_N
- net /DP renamed /USB_DATA_P
- C10 pad 1: /GPS_VCC -> GPS_VCC
- C10 pad 2: Net-(C10-Pad2) -> GND
- C11 pad 1: Net-(C11-Pad1) -> PWR_BUT
- C11 pad 2: /BAT- -> GND
- C12 pad 1: /GPS_VCC -> GPS_VCC
- C13 pad 1: /GPS_VCC -> GPS_VCC
- C5 pad 1: /SD_VCC -> Net-(C5-Pad1)
- C5 pad 2: Net-(C5-Pad2) -> GND
- C7 pad 1: /SD_VCC -> MMC_VCC
- C8 pad 1: /SD_VCC -> MMC_VCC
- IC1 pad 18: /PWR_BUT -> PWR_BUT
- IC1 pad 19: /NEW_BUT -> ~CHG
- IC1 pad 31: /GPS_BACKUP -> GPS_BACKUP
- IC1 pad 32: /GPS_FIX -> Net-(IC1-Pad32)
- IC1 pad 33: /GPS_PPS -> Net-(IC1-Pad33)
- IC1 pad 34: /GPS_PWR -> GPS_PWR
- IC1 pad 35: Net-(IC1-Pad35) -> GPS_PWR_FAULT
- IC1 pad 37: /GPS_MOSI -> Net-(IC1-Pad37)
- IC1 pad 38: /GPS_MISO -> Net-(IC1-Pad38)
- IC1 pad 41: /SD_CLK -> Net-(IC1-Pad41)
- IC1 pad 42: /SD_PWR -> MMC_PWR
- IC1 pad 43: Net-(IC1-Pad43) -> MMC_PWR_FAULT
- IC1 pad 44: /SD_CS -> Net-(IC1-Pad44)
- IC1 pad 45: /SD_MOSI -> Net-(IC1-Pad45)
- IC1 pad 46: /SD_MISO -> Net-(IC1-Pad46)
- IC1 pad 65: (no net) -> GND
- P2 pad 1: GND -> +BATT
- P2 pad 2: /BAT- -> GND
- R10 pad 1: Net-(R10-Pad1) -> PWR_BUT
- R10 pad 2: GND -> Net-(R10-Pad2)
- R11 pad 1: Net-(R11-Pad1) -> MMC_PWR_FAULT
- R11 pad 2: GND -> +3V3
- R5 pad 1: Net-(C5-Pad2) -> Net-(R5-Pad1)
- R5 pad 2: +3V3 -> GPS_VCC
- R6 pad 1: Net-(R6-Pad1) -> GPS_VCC_RF
- R6 pad 2: GND -> Net-(C5-Pad1)
- R8 pad 1: Net-(C10-Pad2) -> GPS_VCC
- R8 pad 2: +BATT -> Net-(R8-Pad2)
- R9 pad 1: Net-(C11-Pad1) -> GPS_PWR_FAULT
- R9 pad 2: +BATT -> +3V3
- SW1 pad 1: /PWR_BUT -> Net-(R10-Pad2)
- U1 pad 1: Net-(R6-Pad1) -> GND
- U1 pad 2: /SD_VCC -> GPS_MISO
- U1 pad 3: /SD_VCC -> GPS_MOSI
- U1 pad 4: +3V3 -> GPS_PPS
- U1 pad 5: /SD_PWR -> Net-(U1-Pad5)
- U1 pad 6: Net-(C5-Pad2) -> GPS_BACKUP
- U2 pad 1: VBUS -> ~CHG
- U3 pad 2: /SD_CS -> MMC_CS
- U3 pad 3: /SD_MOSI -> MMC_MOSI
- U3 pad 4: /SD_VCC -> MMC_VCC
- U3 pad 5: /SD_CLK -> MMC_CLK
- U3 pad 7: /SD_MISO -> MMC_MISO
- U4 pad 1: Net-(R10-Pad1) -> +3V3
- U4 pad 2: /GPS_VCC -> GND
- U4 pad 3: /GPS_VCC -> GPS_PWR
- U4 pad 4: +BATT -> GPS_PWR_FAULT
- U4 pad 5: /GPS_PWR -> Net-(L2-Pad1)
- U5 pad 1: Net-(Q1-Pad4) -> +3V3
- U5 pad 2: Net-(R11-Pad1) -> GND
- U5 pad 3: Net-(Q1-Pad5) -> MMC_PWR
- U5 pad 4: Net-(U5-Pad4) -> MMC_PWR_FAULT
- U5 pad 5: Net-(C11-Pad1) -> Net-(L3-Pad1)
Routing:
- net VBUS: track 111.8 -> 44.1 mm, vias 4 -> 3
- net GPS_BACKUP: track 0.00 -> 49.1 mm, vias 0 -> 2
- net /SD_PWR: track 44.1 -> 0.00 mm
- net GPS_MOSI: track 0.00 -> 42.9 mm, vias 0 -> 2
- net GPS_PPS: track 0.00 -> 42.5 mm, vias 0 -> 2
- net /GPS_PWR: track 42.4 -> 0.00 mm, vias 4 -> 0
- net /LED_A_R: track 46.1 -> 4.14 mm, vias 2 -> 0
- net GPS_MISO: track 0.00 -> 41.6 mm, vias 0 -> 2
- net GND: track 48.0 -> 89.6 mm, vias 4 -> 17
- net /LED_B_R: track 43.4 -> 3.71 mm, vias 2 -> 0
- net GPS_VCC: track 0.00 -> 38.1 mm, vias 0 -> 3
- net GPS_PWR_FAULT: track 0.00 -> 37.9 mm, vias 0 -> 2
- net /LED_B_G: track 42.3 -> 5.15 mm, vias 2 -> 0
- net /LED_A_B: track 42.9 -> 6.50 mm, vias 2 -> 0
- net /LED_B_B: track 43.1 -> 6.74 mm, vias 2 -> 0
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- added copper zone on B.Cu, net /ANT_RF
- added copper zone on In2.Cu, net GND
- added copper zone on B.Cu, net Net-(C21-Pad1)
- added copper zone on B.Cu, net Net-(C21-Pad2)
- added copper zone on B.Cu, net Net-(C22-Pad2)
- added copper zone on B.Cu, net Net-(L4-Pad2)
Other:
- outline, holes or cut-outs redrawn
- copper layers 2 -> 4
- net class Power: clearance 0.2 -> 0.22
- net class USB added: clearance 0.177, trace_width 0.177, via_dia 0.7, via_drill 0.3
- rule trace_min: 0.18 -> 0.15
- board text added: "gpsLogger"
- board text added: "v2.1"
- board text removed: "BAT+"
- board text removed: "BAT-"
- board text removed: "Gnd"
- board text removed: "github.com/Greeeg/gpsLogger"

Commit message: Merge PCB changes from Mark3 branch.
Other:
- rule pad_to_mask_clearance: 0.2 -> 0.05
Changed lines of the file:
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@@
-(kicad_pcb (version 4) (host pcbnew 4.0.2-stable)
+(kicad_pcb (version 20171130) (host pcbnew "(5.0.0-rc2-dev-321-g78161b592)")
   (general
-    (links 342)
-    (no_connects 0)
-    (area -81.418183 56.392421 174.000001 148.634556)
     (thickness 1.6)
     (drawings 28)
@@
     (47 F.CrtYd user)
     (48 B.Fab user)
-    (49 F.Fab user)
+    (49 F.Fab user hide)
   )
   (setup
@@
     (pad_size 1.8375 1.8375)
     (pad_drill 0)
-    (pad_to_mask_clearance 0.2)
+    (pad_to_mask_clearance 0.05)
     (aux_axis_origin 151.5 102.5)
     (visible_elements 7FFFFFFF)
@@
       (layerselection 0x01000_80000000)
       (usegerberextensions false)
+      (usegerberattributes false)
+      (usegerberadvancedattributes false)
+      (creategerberjobfile false)
       (excludeedgelayer true)
       (linewidth 0.100000)
@@
       (hpglpenspeed 20)
       (hpglpendiameter 15)
-      (hpglpenoverlay 2)
       (psnegative false)
       (psa4output false)
@@
     (pad 6 thru_hole oval (at 3.65 0.7 355) (size 1 1) (drill 0.65) (layers *.Cu *.Mask)
       (net 2 GND))
-    (pad 6 thru_hole oval (at 3.65 -0.95 355) (size 1 1) (drill 0.65) (layers *.Cu *.Mask)
+    (pad 6 thru_hole oval (at 3.65 -0.950001 355) (size 1 1) (drill 0.65) (layers *.Cu *.Mask)
       (net 2 GND))
     (pad 6 thru_hole oval (at 3.65 0.35 355) (size 1 1) (drill 0.65) (layers *.Cu *.Mask)
